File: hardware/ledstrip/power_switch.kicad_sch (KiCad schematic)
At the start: 9 parts, among them SW1 SW_SPST, U8 TPS25940

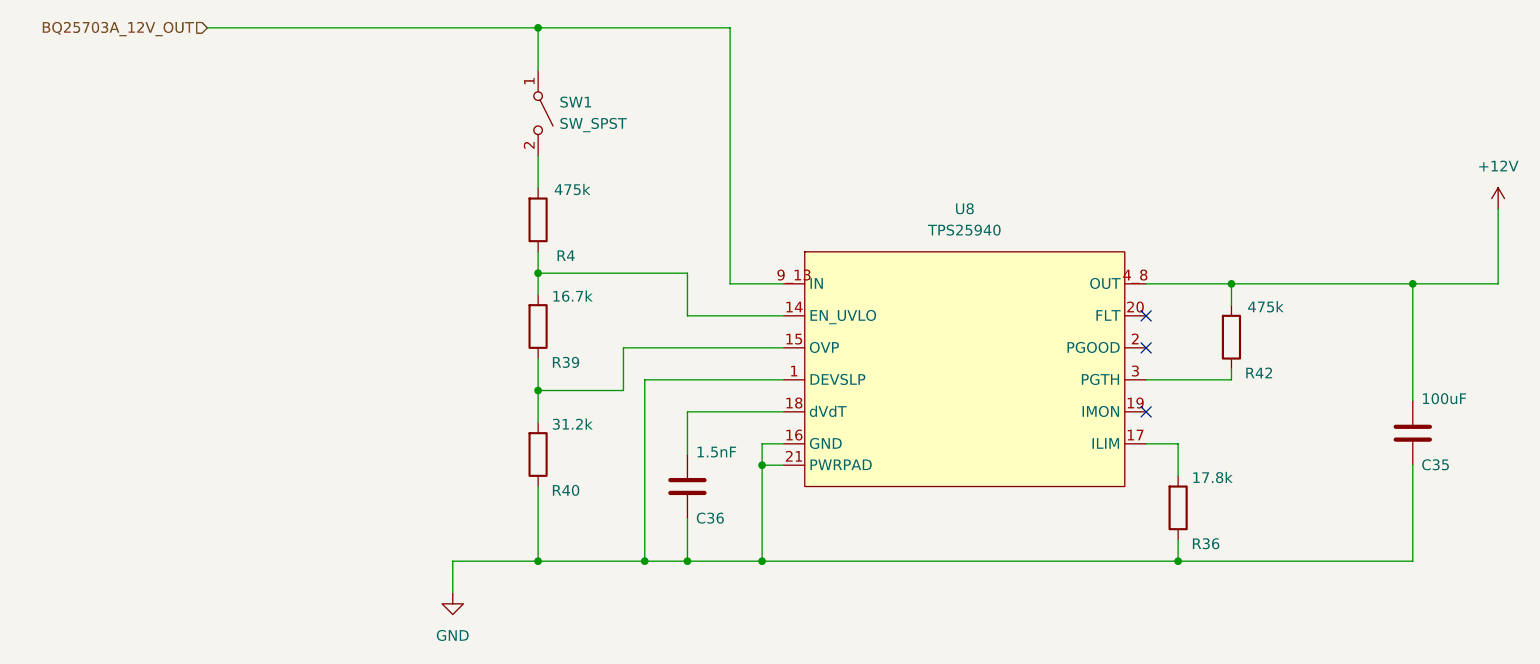
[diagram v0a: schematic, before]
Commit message: Add a lot of TestPoints
Move P-FET at the edge of board.
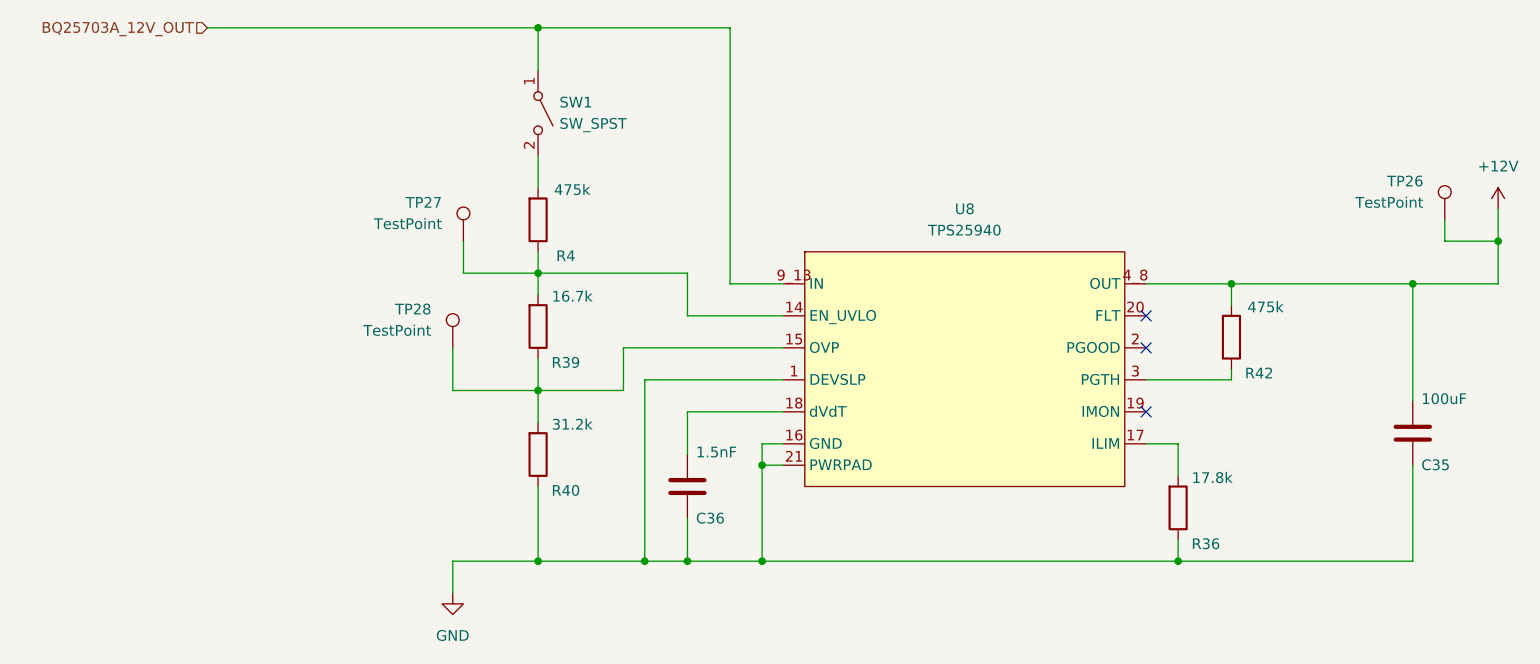
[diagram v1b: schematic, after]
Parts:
- added TP26, TP27, TP28: TestPoint, TestPoint:TestPoint_Pad_1.0x1.0mm, symbol Connector:TestPoint
- U8: footprint Package_DFN_QFN:QFN-20-1EP_3x4mm_P0.5mm_EP1.65x2.65mm_ThermalVias -> ledstrip:QFN-20-1EP_3x4mm_P0.5mm_EP1.65x2.65mm_ThermalVias_PROJECTCOPY
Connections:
- net +12V: now also TP26.1
- net at R39.1, R40.2, U8.15 (OVP): now also TP28.1
- net at R39.2, R4.1, U8.14 (EN_UVLO): now also TP27.1

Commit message: Add MPN and stuff to TPS25940
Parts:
- U8: Distributor Link 1 (none) -> https://www.mouser.fr/ProductDetail/Texas-Instruments/TPS25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; MPN (none) -> TPS25940ARVCT; Manufacturer (none) -> Texas Instrument
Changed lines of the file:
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@@
+			)
+		)
+		(property "Distributor Link 1" "https://www.mouser.fr/ProductDetail/Texas-Instruments/TPS25940ARVCT?qs=1MXlzafEN39WRT24Wg%2FJYg%3D%3D"
+			(at 125.73 106.68 0)
+			(effects
+				(font
+					(size 1.27 1.27)
+				)
+				(hide yes)
+			)
+		)
+		(property "Manufacturer" "Texas Instrument"
+			(at 125.73 106.68 0)
+			(effects
+				(font
+					(size 1.27 1.27)
+				)
+				(hide yes)
+			)
+		)
+		(property "MPN" "TPS25940ARVCT"
+			(at 125.73 106.68 0)
+			(effects
+				(font
+					(size 1.27 1.27)
+				)
+				(hide yes)
 			)
 		)

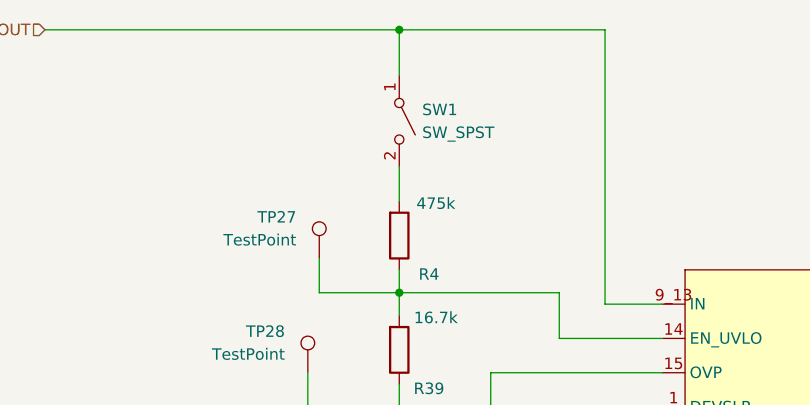
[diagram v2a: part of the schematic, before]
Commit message: Improve BOM: exclude uneeded parts, add some columns.
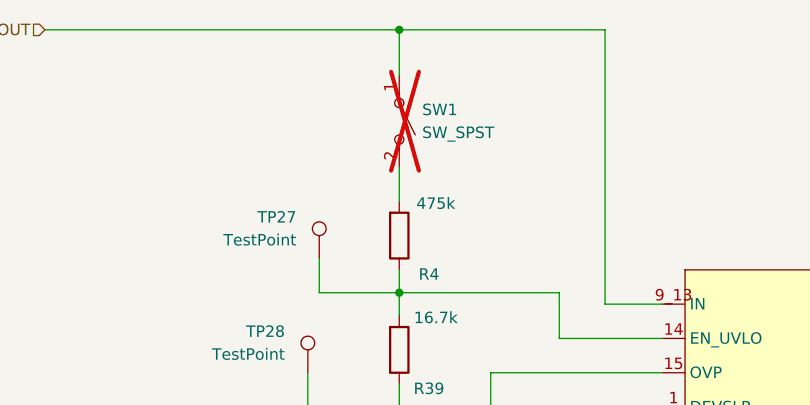
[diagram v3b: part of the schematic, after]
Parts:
- SW1: now not fitted
- TP26, TP27, TP28: now left out of the parts list
